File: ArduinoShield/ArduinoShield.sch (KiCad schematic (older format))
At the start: 2 parts, among them J1 Conn_02x20_Odd_Even

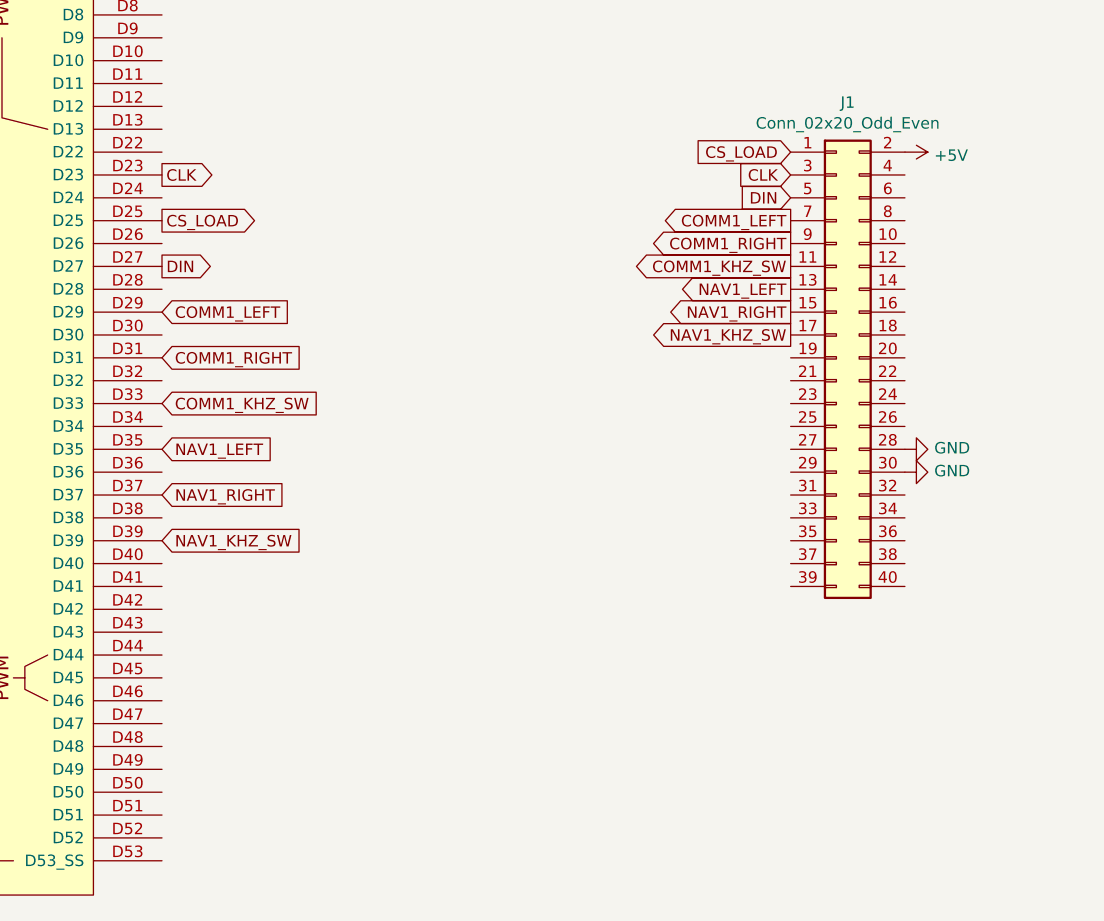
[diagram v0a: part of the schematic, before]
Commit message: Remaining encoders and some buttons confirmed
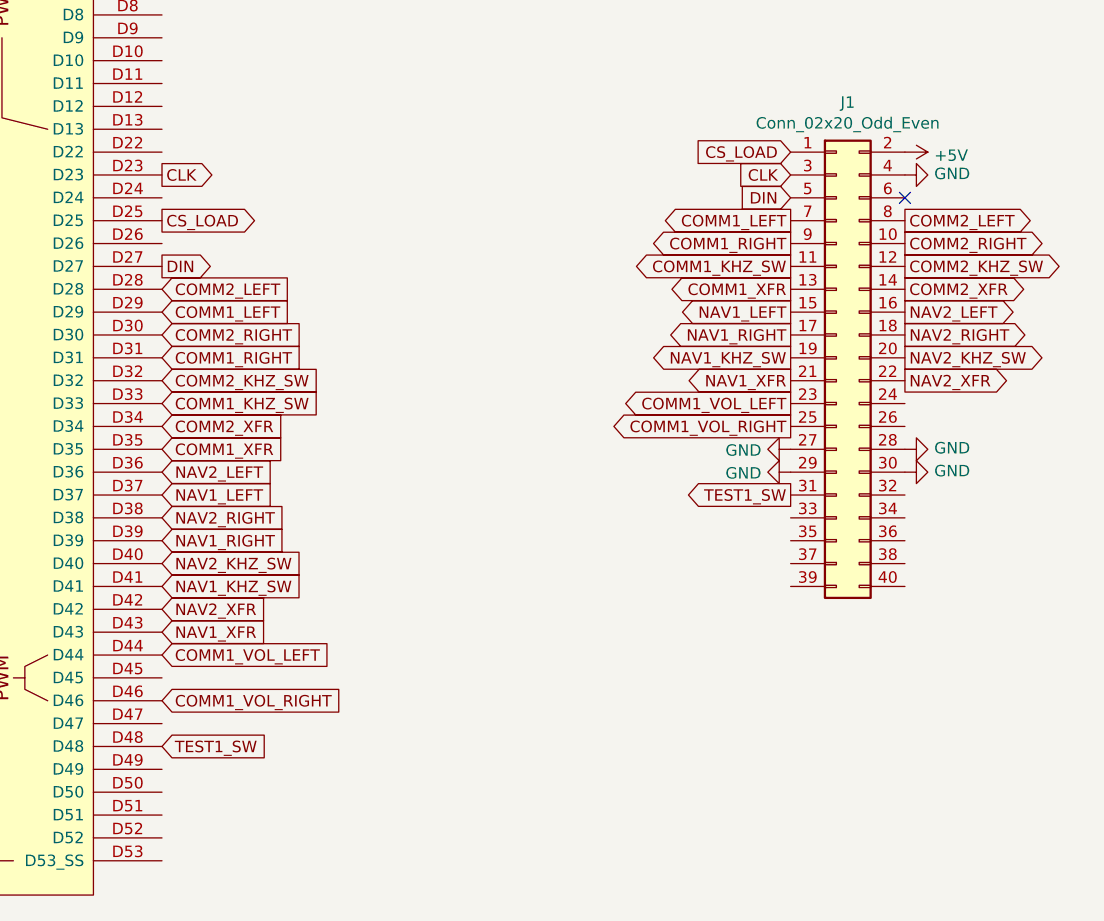
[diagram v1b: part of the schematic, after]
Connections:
- net GND: now also J1.27 (Pin_27), J1.29 (Pin_29), J1.4 (Pin_4)
- net NAV1_KHZ_SW: now also J1.19 (Pin_19), XA1.D41; no longer J1.17 (Pin_17), XA1.D39
- net NAV1_LEFT: now also J1.15 (Pin_15), XA1.D37; no longer J1.13 (Pin_13), XA1.D35
- net NAV1_RIGHT: now also J1.17 (Pin_17), XA1.D39; no longer J1.15 (Pin_15), XA1.D37
- net COMM2_LEFT: now reaches XA1.D28
- net COMM2_LEFT: now also J1.8 (Pin_8)
- net COMM2_RIGHT: now reaches XA1.D30
- net COMM2_RIGHT: now also J1.10 (Pin_10)
- net COMM2_KHZ_SW: now reaches XA1.D32
- net COMM2_KHZ_SW: now also J1.12 (Pin_12)
- net COMM2_XFR: now reaches XA1.D34
- net COMM2_XFR: now also J1.14 (Pin_14)
- net NAV2_LEFT: now reaches XA1.D36
- net NAV2_LEFT: now also J1.16 (Pin_16)
- net NAV2_RIGHT: now reaches XA1.D38
- net NAV2_RIGHT: now also J1.18 (Pin_18)
- net NAV2_KHZ_SW: now reaches XA1.D40
- net NAV2_KHZ_SW: now also J1.20 (Pin_20)
- net NAV2_XFR: now reaches XA1.D42
- net NAV2_XFR: now also J1.22 (Pin_22)
- net NAV1_XFR: now reaches XA1.D43
- net NAV1_XFR: now also J1.21 (Pin_21)
- net COMM1_VOL_LEFT: now reaches XA1.D44
- net COMM1_VOL_LEFT: now also J1.23 (Pin_23)
- net COMM1_VOL_RIGHT: now reaches XA1.D46
- net COMM1_VOL_RIGHT: now also J1.25 (Pin_25)
- net TEST1_SW: now reaches XA1.D48
- net TEST1_SW: now also J1.31 (Pin_31)
- new net COMM1_XFR: J1.13 (Pin_13), XA1.D35
- no-connect marks 6 -> 7
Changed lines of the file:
@@
 Text GLabel 4700 3650 2    50   Input ~ 0
 COMM1_RIGHT
+Text GLabel 7450 3450 0    50   Output ~ 0
+NAV1_LEFT
+Text GLabel 7450 3550 0    50   Output ~ 0
+NAV1_RIGHT
+Text GLabel 7450 3650 0    50   Output ~ 0
+NAV1_KHZ_SW
+Text GLabel 4700 4250 2    50   Input ~ 0
+NAV1_LEFT
+Text GLabel 4700 4450 2    50   Input ~ 0
+NAV1_RIGHT
+Text GLabel 4700 4650 2    50   Input ~ 0
+NAV1_KHZ_SW
+Text GLabel 4700 4950 2    50   Input ~ 0
+COMM1_VOL_LEFT
+Text GLabel 4700 5150 2    50   Input ~ 0
+COMM1_VOL_RIGHT
+Text GLabel 7450 3850 0    50   Output ~ 0
+COMM1_VOL_LEFT
+Text GLabel 7450 3950 0    50   Output ~ 0
+COMM1_VOL_RIGHT
+$Comp
+L power:GND #PWR?
+U 1 1 5F6A5DCE
+P 7450 4050
+F 0 "#PWR?" H 7450 3800 50  0001 C CNN
+F 1 "GND" V 7455 3922 50  0000 R CNN
+F 2 "" H 7450 4050 50  0001 C CNN
+F 3 "" H 7450 4050 50  0001 C CNN
+	1    7450 4050
+	0    1    1    0
+$EndComp
+$Comp
+L power:GND #PWR?
+U 1 1 5F6A618F
+P 7450 4150
+F 0 "#PWR?" H 7450 3900 50  0001 C CNN
+F 1 "GND" V 7455 4022 50  0000 R CNN
+F 2 "" H 7450 4150 50  0001 C CNN
+F 3 "" H 7450 4150 50  0001 C CNN
+	1    7450 4150
+	0    1    1    0
+$EndComp
+Text GLabel 7450 4250 0    50   Output ~ 0
+TEST1_SW
+Text GLabel 4700 5350 2    50   Input ~ 0
+TEST1_SW
+Text GLabel 7950 3050 2    50   Output ~ 0
+COMM2_LEFT
+Text GLabel 7950 3150 2    50   Output ~ 0
+COMM2_RIGHT
+Text GLabel 7950 3250 2    50   Output ~ 0
+COMM2_KHZ_SW
+Text GLabel 4700 3350 2    50   Input ~ 0
+COMM2_LEFT
+Text GLabel 4700 3550 2    50   Input ~ 0
+COMM2_RIGHT
+Text GLabel 4700 3750 2    50   Input ~ 0
+COMM2_KHZ_SW
+$Comp
+L power:GND #PWR?
+U 1 1 5F6A881F
+P 7950 2850
+F 0 "#PWR?" H 7950 2600 50  0001 C CNN
+F 1 "GND" V 7955 2722 50  0000 R CNN
+F 2 "" H 7950 2850 50  0001 C CNN
+F 3 "" H 7950 2850 50  0001 C CNN
+	1    7950 2850
+	0    -1   -1   0
+$EndComp
+NoConn ~ 7950 2950
+Text GLabel 7950 3350 2    50   Output ~ 0
+COMM2_XFR
 Text GLabel 7450 3350 0    50   Output ~ 0
-NAV1_LEFT
-Text GLabel 7450 3450 0    50   Output ~ 0
-NAV1_RIGHT
-Text GLabel 7450 3550 0    50   Output ~ 0
-NAV1_KHZ_SW
+COMM1_XFR
+Text GLabel 7450 3750 0    50   Output ~ 0
+NAV1_XFR
+Text GLabel 4700 4150 2    50   Input ~ 0
+NAV2_LEFT
+Text GLabel 4700 4350 2    50   Input ~ 0
+NAV2_RIGHT
+Text GLabel 4700 4550 2    50   Input ~ 0
+NAV2_KHZ_SW
+Text GLabel 4700 3950 2    50   Input ~ 0
+COMM2_XFR
 Text GLabel 4700 4050 2    50   Input ~ 0
-NAV1_LEFT
-Text GLabel 4700 4250 2    50   Input ~ 0
-NAV1_RIGHT
-Text GLabel 4700 4450 2    50   Input ~ 0
-NAV1_KHZ_SW
+COMM1_XFR
+Text GLabel 7950 3450 2    50   Output ~ 0
+NAV2_LEFT
+Text GLabel 7950 3550 2    50   Output ~ 0
+NAV2_RIGHT
+Text GLabel 7950 3650 2    50   Output ~ 0
+NAV2_KHZ_SW
+Text GLabel 7950 3750 2    50   Output ~ 0
+NAV2_XFR
+Text GLabel 4700 4750 2    50   Input ~ 0
+NAV2_XFR
+Text GLabel 4700 4850 2    50   Input ~ 0
+NAV1_XFR
 $EndSCHEMATC

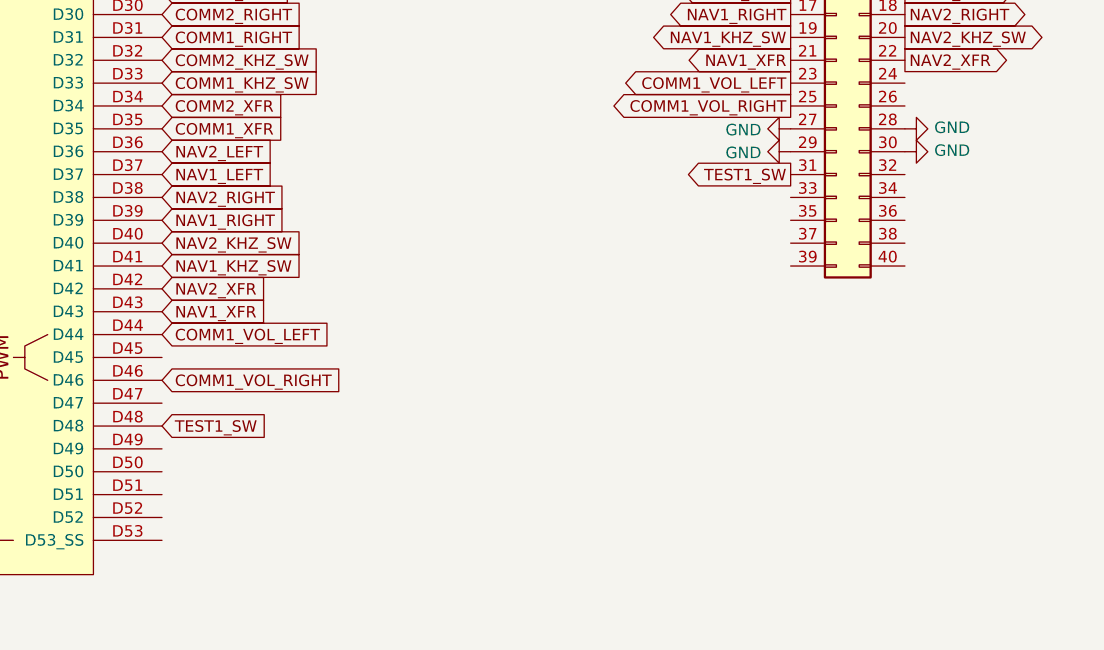
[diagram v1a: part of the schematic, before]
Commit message: All comm and nav radio freq set and swap tested
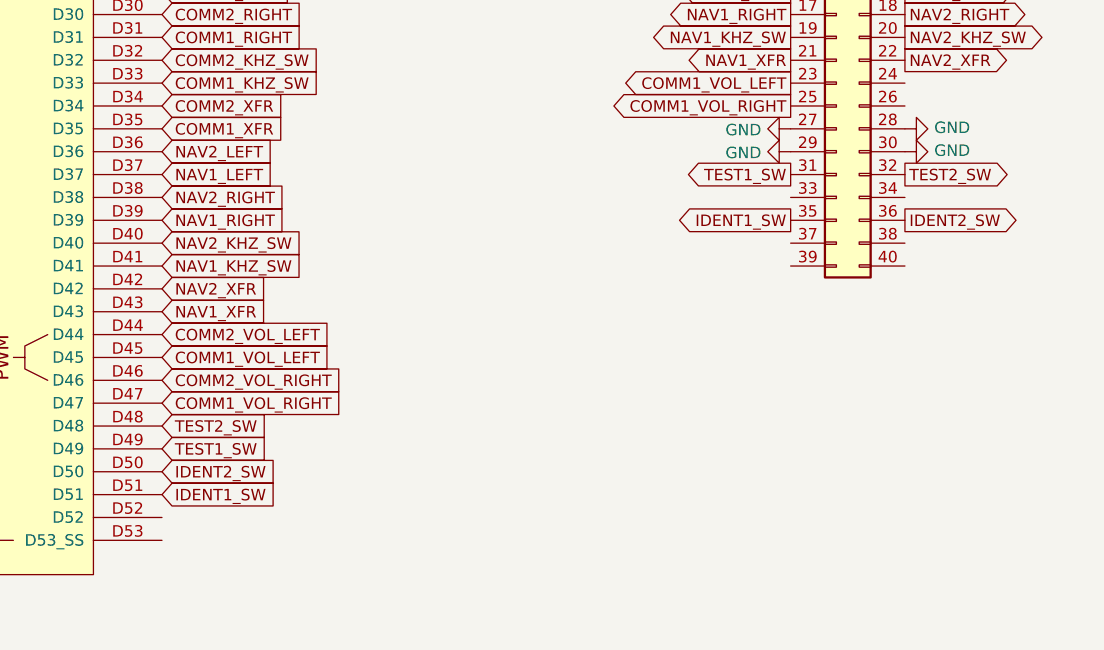
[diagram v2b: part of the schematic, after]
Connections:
- net COMM1_VOL_LEFT: now also XA1.D45; no longer XA1.D44
- net COMM1_VOL_RIGHT: now also XA1.D47; no longer XA1.D46
- net TEST1_SW: now also XA1.D49; no longer XA1.D48
- net IDENT2_SW: now reaches XA1.D50
- net IDENT2_SW: now also J1.36 (Pin_36)
- net IDENT1_SW: now reaches XA1.D51
- net IDENT1_SW: now also J1.35 (Pin_35)
- net TEST2_SW: now reaches J1.32 (Pin_32)
- net TEST2_SW: now also XA1.D48
- new net COMM2_VOL_LEFT: XA1.D44
- new net COMM2_VOL_RIGHT: XA1.D46
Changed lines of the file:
@@
 Text GLabel 4700 4650 2    50   Input ~ 0
 NAV1_KHZ_SW
-Text GLabel 4700 4950 2    50   Input ~ 0
+Text GLabel 4700 5050 2    50   Input ~ 0
 COMM1_VOL_LEFT
-Text GLabel 4700 5150 2    50   Input ~ 0
+Text GLabel 4700 5250 2    50   Input ~ 0
 COMM1_VOL_RIGHT
 Text GLabel 7450 3850 0    50   Output ~ 0
@@
 Text GLabel 7450 4250 0    50   Output ~ 0
 TEST1_SW
-Text GLabel 4700 5350 2    50   Input ~ 0
+Text GLabel 4700 5450 2    50   Input ~ 0
 TEST1_SW
 Text GLabel 7950 3050 2    50   Output ~ 0
@@
 Text GLabel 4700 4850 2    50   Input ~ 0
 NAV1_XFR
+Text GLabel 4700 5350 2    50   Input ~ 0
+TEST2_SW
+Text GLabel 7950 4250 2    50   Output ~ 0
+TEST2_SW
+Text GLabel 7950 4450 2    50   Output ~ 0
+IDENT2_SW
+Text GLabel 4700 5650 2    50   Input ~ 0
+IDENT1_SW
+Text GLabel 4700 5550 2    50   Input ~ 0
+IDENT2_SW
+Text GLabel 7450 4450 0    50   Output ~ 0
+IDENT1_SW
+Text GLabel 4700 4950 2    50   Input ~ 0
+COMM2_VOL_LEFT
+Text GLabel 4700 5150 2    50   Input ~ 0
+COMM2_VOL_RIGHT
 $EndSCHEMATC
